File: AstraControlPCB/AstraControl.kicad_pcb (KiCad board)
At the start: 4 copper layers, 102 x 96 mm, 154 parts, among them CN1 4P JST VH, CN10 JST_ZH_6PIN_1A_250V, CN2 4P JST VH, CN3 4P JST VH, CN4 4P JST ZH, CN5 4P JST ZH, CN6 4P JST ZH, CN7 JST_VH_8PIN_10A_250V, CN8 4P JST ZH, CN9 4P JST ZH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

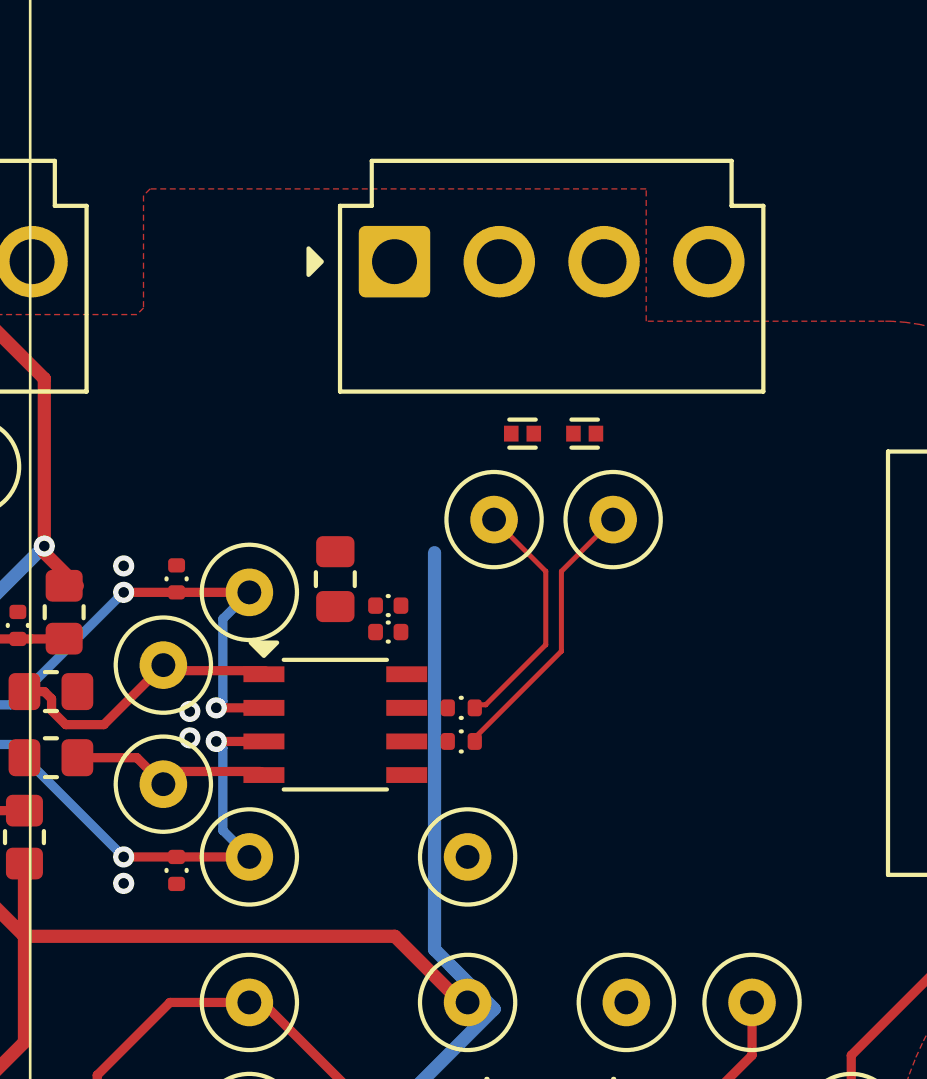
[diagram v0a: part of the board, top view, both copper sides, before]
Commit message: RS485 tranceiver changed and TVS
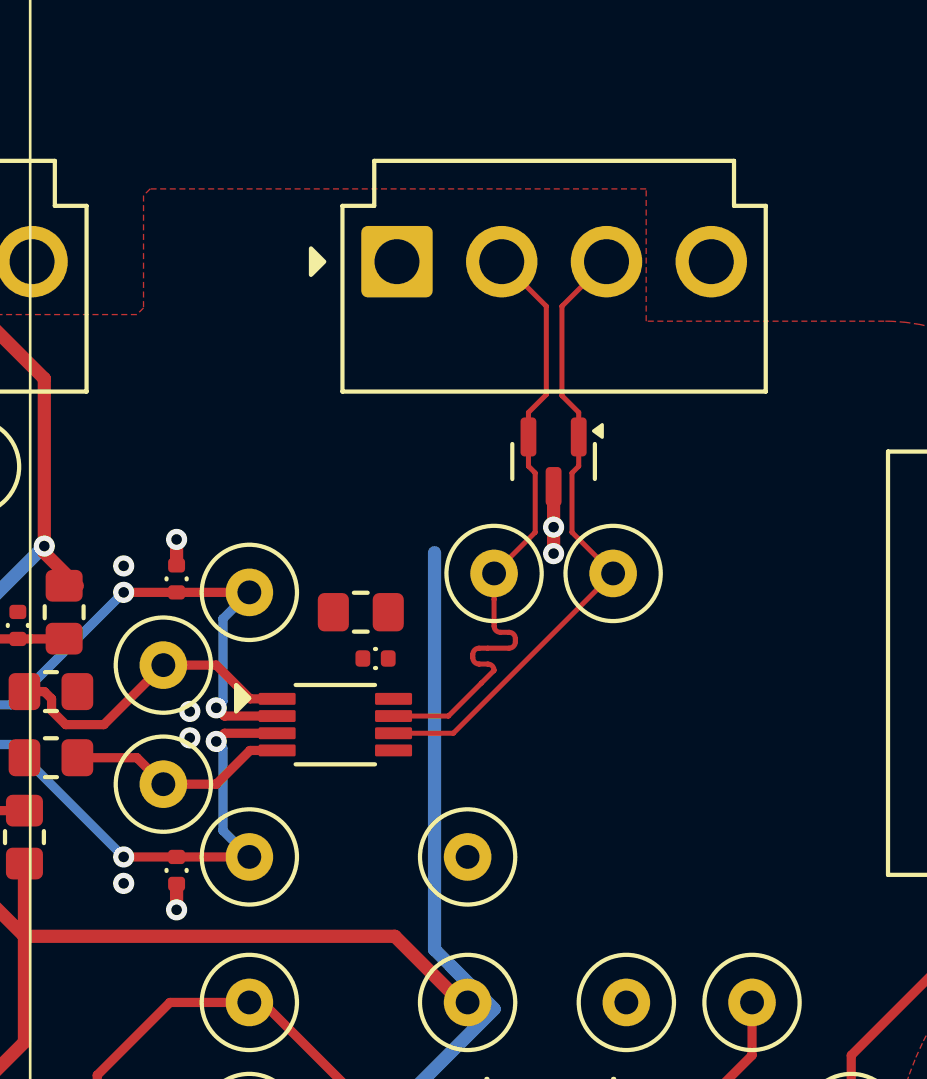
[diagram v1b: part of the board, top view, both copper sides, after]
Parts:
- removed C19: 100n, LiveAstra:C_0402_1005Metric
- removed D2: H5VL10B, LiveAstra:D_DFN0603_H5VL10B_Bidirectional_TVS
- removed R14, R15: 10, LiveAstra:R_0402_1005Metric
- D3: value H5VL10B -> NUP3105LT1G; footprint LiveAstra:D_DFN0603_H5VL10B_Bidirectional_TVS -> LiveAstra:TVS_NUP3105LT1G_36V
- U5: value SN65HVD1782DR -> THVD2450DGKR; footprint LiveAstra:RS_485_SN65HVD1782DR -> LiveAstra:THVD2450DGKR_RS485_Transciever_VSSOP8
- moved TP15 2.03 mm to (172.3, 57.2)
- moved TP16 2.03 mm to (167.8, 57.2)
- moved D3 1.64 mm to (170.0, 53.0), turned to -90 degrees
- moved C17 1.58 mm to (162.7, 58.6), turned to 0 degrees
- moved C18 1.11 mm to (163.3, 60.4)
- moved CN1 0.09 mm to (164.1, 45.4)
- turned U5 to 0 degrees
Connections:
- C17 pad 2: +3V3 -> +5V
- C18 pad 2: +3V3 -> +5V
- CN1 pad 2: /Block Diagram/Power Connectors/RS485_D+ -> /Block Diagram/UART to RS-485/RS485_IC_D+
- CN1 pad 3: /Block Diagram/Power Connectors/RS485_D- -> /Block Diagram/UART to RS-485/RS485_IC_D-
- D3 pad 1: GND -> /Block Diagram/UART to RS-485/RS485_IC_D-
- D3 pad 2: /Block Diagram/Power Connectors/RS485_D- -> /Block Diagram/UART to RS-485/RS485_IC_D+
- TP15 pad 1: /Block Diagram/Power Connectors/RS485_D- -> /Block Diagram/UART to RS-485/RS485_IC_D-
- TP16 pad 1: /Block Diagram/Power Connectors/RS485_D+ -> /Block Diagram/UART to RS-485/RS485_IC_D+
- U5 pad 8: +3V3 -> +5V
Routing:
- net /Block Diagram/UART to RS-485/RS485_IC_D-: track 0.00 -> 24.3 mm
- net /Block Diagram/UART to RS-485/RS485_IC_D+: track 0.00 -> 24.2 mm
- net /Block Diagram/Power Connectors/RS485_D-: track 10.4 -> 0.00 mm
- net /Block Diagram/Power Connectors/RS485_D+: track 9.16 -> 0.00 mm
- net GND: track 20.2 -> 24.7 mm, vias 63 -> 67
- net /Block Diagram/UART to RS-485/RS485_RX_IC: track 11.0 -> 11.9 mm
- net /Block Diagram/UART to RS-485/RS485_TX_IC: track 7.72 -> 8.49 mm
- net /Block Diagram/MCU/GPIO_6_RS485_RE: track 38.1 -> 38.7 mm
- net /Block Diagram/MCU/GPIO_5_RS485_DE: track 35.8 -> 36.4 mm

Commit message: Reroute complete
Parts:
- added C19: 47u, LiveAstra:C_0805_2012Metric_Pad1.18x1.45mm_HandSolder, F.Cu at (144.8, 68.1)
- added C28: DNP, LiveAstra:C_0805_2012Metric_Pad1.18x1.45mm_HandSolder, F.Cu at (173.0, 75.6)
- added R14: 1M, LiveAstra:R_0805_2012Metric_Pad1.20x1.40mm_HandSolder, F.Cu at (179.5, 99.9)
- C1: value 22u -> 47u; footprint LiveAstra:C_0603_1608Metric -> LiveAstra:C_0805_2012Metric_Pad1.18x1.45mm_HandSolder
- moved R45 113.1 mm to (105.8, 111.6), turned to -90 degrees
- moved C25 108.0 mm to (108.8, 111.6), turned to -90 degrees
- moved C24 73.6 mm to (172.8, 37.4), turned to 0 degrees
- moved R44 67.8 mm to (167.5, 37.4), turned to 180 degrees
- moved C27 60.7 mm to (104.6, 48.9), turned to 180 degrees
- moved R47 53.4 mm to (104.5, 51.4), turned to 180 degrees
- moved TP10 53.4 mm to (117.0, 68.1)
- moved TP11 42.4 mm to (104.8, 69.8)
- moved C1 22.9 mm to (163.0, 55.9), turned to 0 degrees
- moved C17 17.5 mm to (166.8, 75.6), turned to 180 degrees
- moved CN4 12.0 mm to (184.3, 119.6)
- moved CN5 12.0 mm to (172.3, 119.6)
- moved TP33 12.0 mm to (167.8, 114.6)
- moved TP35 12.0 mm to (179.8, 114.6)
- moved TP36 12.0 mm to (184.3, 114.6)
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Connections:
- C1 pad 2: +3V3 -> +5V
- C17 pad 2: +5V -> +3V3
- CN1 pad 2: /Block Diagram/UART to RS-485/RS485_IC_D+ -> /Block Diagram/Power Connectors/RS485_D+
- CN1 pad 3: /Block Diagram/UART to RS-485/RS485_IC_D- -> /Block Diagram/Power Connectors/RS485_D-
- D3 pad 1: /Block Diagram/UART to RS-485/RS485_IC_D- -> /Block Diagram/Power Connectors/RS485_D+
- D3 pad 2: /Block Diagram/UART to RS-485/RS485_IC_D+ -> /Block Diagram/Power Connectors/RS485_D-
- TP15 pad 1: /Block Diagram/UART to RS-485/RS485_IC_D- -> /Block Diagram/Power Connectors/RS485_D-
- TP16 pad 1: /Block Diagram/UART to RS-485/RS485_IC_D+ -> /Block Diagram/Power Connectors/RS485_D+
- U1 pad 28: /Block Diagram/Fan, Temperature and Screen/FAN_PWM -> /Block Diagram/Fan, Temperature and Screen/TEMP_I2C_SCL
- U1 pad 29: /Block Diagram/Fan, Temperature and Screen/FAN_TACHO -> /Block Diagram/Fan, Temperature and Screen/TEMP_I2C_SDA
- U1 pad 30: /Block Diagram/Fan, Temperature and Screen/TEMP_I2C_SCL -> /Block Diagram/Fan, Temperature and Screen/FAN_PWM
- U1 pad 31: /Block Diagram/Fan, Temperature and Screen/TEMP_I2C_SDA -> /Block Diagram/Fan, Temperature and Screen/FAN_TACHO
- U2 pad 4: unconnected-(U2-~{FLAG}-Pad4) -> /Block Diagram/5V Protection/FLAG_IC
- U5 pad 6: /Block Diagram/UART to RS-485/RS485_IC_D- -> /Block Diagram/Power Connectors/RS485_D-
- U5 pad 7: /Block Diagram/UART to RS-485/RS485_IC_D+ -> /Block Diagram/Power Connectors/RS485_D+
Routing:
- net +3V3: track 103.4 -> 22.6 mm, vias 12 -> 39
- net GND: track 24.7 -> 65.9 mm, vias 67 -> 125
- net /Block Diagram/UART to RS-485/RS485_IC_D-: track 24.3 -> 0.00 mm
- net /Block Diagram/UART to RS-485/RS485_IC_D+: track 24.2 -> 0.00 mm
- net /Block Diagram/Power Connectors/RS485_D-: track 0.00 -> 24.1 mm
- net /Block Diagram/Power Connectors/RS485_D+: track 0.00 -> 24.0 mm
- net /Block Diagram/3V3 to 5V Logic Shifter/5V_IO_1: track 8.22 -> 26.3 mm
- net /Block Diagram/3V3 to 5V Logic Shifter/5V_IO_4: track 20.5 -> 33.4 mm
- net /Block Diagram/3V3 to 5V Logic Shifter/OE_IC: track 0.00 -> 12.2 mm
- net /Block Diagram/MCU/IO_3_IC: track 0.00 -> 10.0 mm
- net /Block Diagram/5V Protection/FLAG_IC: track 0.00 -> 8.66 mm, vias 0 -> 2
- net CHASSIS: track 0.00 -> 8.37 mm
- net /Block Diagram/3V3 to 5V Logic Shifter/5V_IO_3: track 24.3 -> 32.3 mm
- net /Block Diagram/5V to 3.3V/SW_OUT_UNFILTERED: track 10.2 -> 17.5 mm
- net /Block Diagram/Fan, Temperature and Screen/FAN_TACHO: track 10.8 -> 17.4 mm
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- added copper zone on B.Cu, net +5V
- added copper zone on B.Cu, net +5V_IN
- added copper zone on B.Cu, net /Block Diagram/Power Connectors/USB/VBUS
- added copper zone on F.Cu, net /Block Diagram/Power Connectors/USB/VBUS
- added copper zone on F.Cu, net CHASSIS

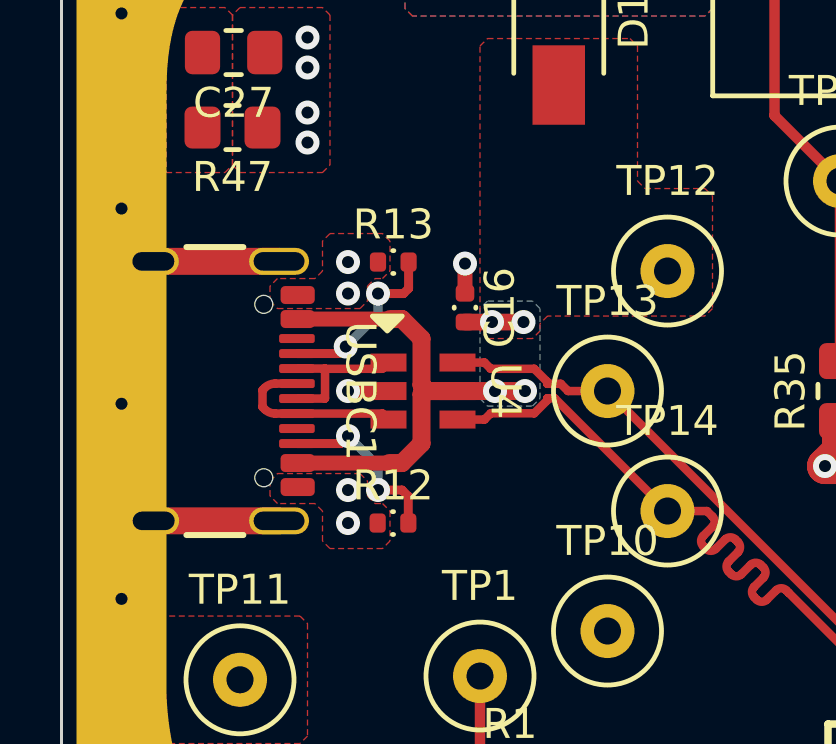
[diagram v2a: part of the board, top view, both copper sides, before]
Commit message: Fixed fab layer
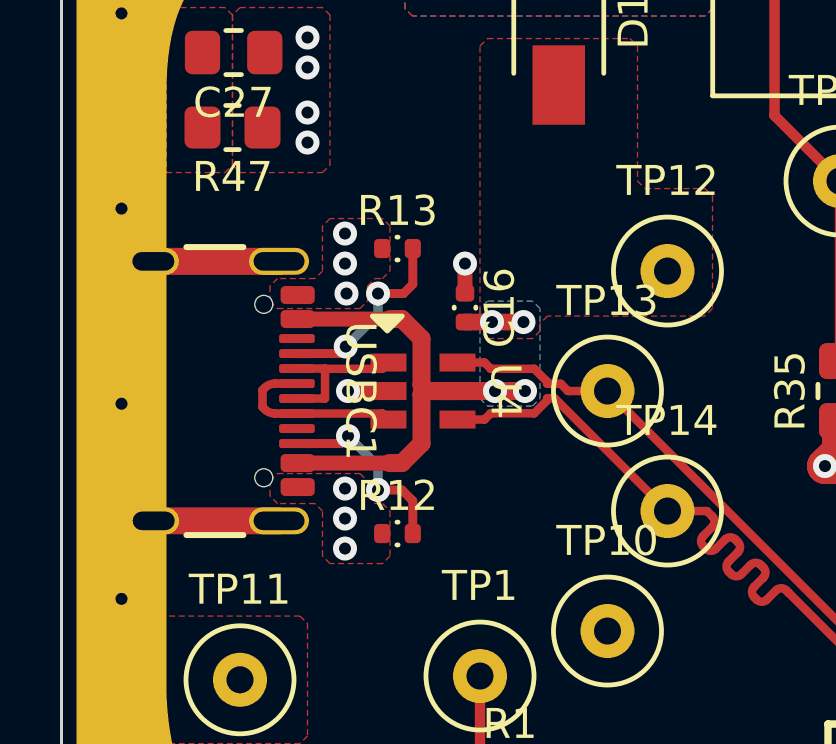
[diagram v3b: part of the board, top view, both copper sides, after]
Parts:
- C12, C15, C17, C28: footprint LiveAstra:C_0805_2012Metric_Pad1.18x1.45mm_HandSolder -> LiveAstra:C_DNP_0805_2012Metric_Pad1.18x1.45mm_HandSolder
- R26, R27, R33, R34, R45, R46, R47, R48, R49: footprint LiveAstra:R_0805_2012Metric_Pad1.20x1.40mm_HandSolder -> LiveAstra:R_DNP_0805_2012Metric_Pad1.20x1.40mm_HandSolder
- moved R13 0.47 mm to (110.0, 55.4)
- moved R12 0.38 mm to (110.0, 64.9)
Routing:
- net /Block Diagram/Power Connectors/USB/CC1: track 5.91 -> 6.41 mm
- net GND: vias 125 -> 127

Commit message: Silkscreen
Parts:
- moved R1 3.72 mm to (117.3, 71.6)
- moved D1 0.16 mm to (115.3, 47.9)
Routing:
- net +3V3: track 22.6 -> 27.0 mm
- net /Block Diagram/MCU/IO_3_IC: track 10.0 -> 7.03 mm
- net /Block Diagram/MCU/IO_3_TEST: track 3.25 -> 4.33 mm
- net /Block Diagram/Fan, Temperature and Screen/TEMP_I2C_SCL: track 67.2 -> 66.2 mm
- net /Block Diagram/Fan, Temperature and Screen/TEMP_I2C_SDA: track 71.7 -> 71.1 mm
- net GND: vias 127 -> 129

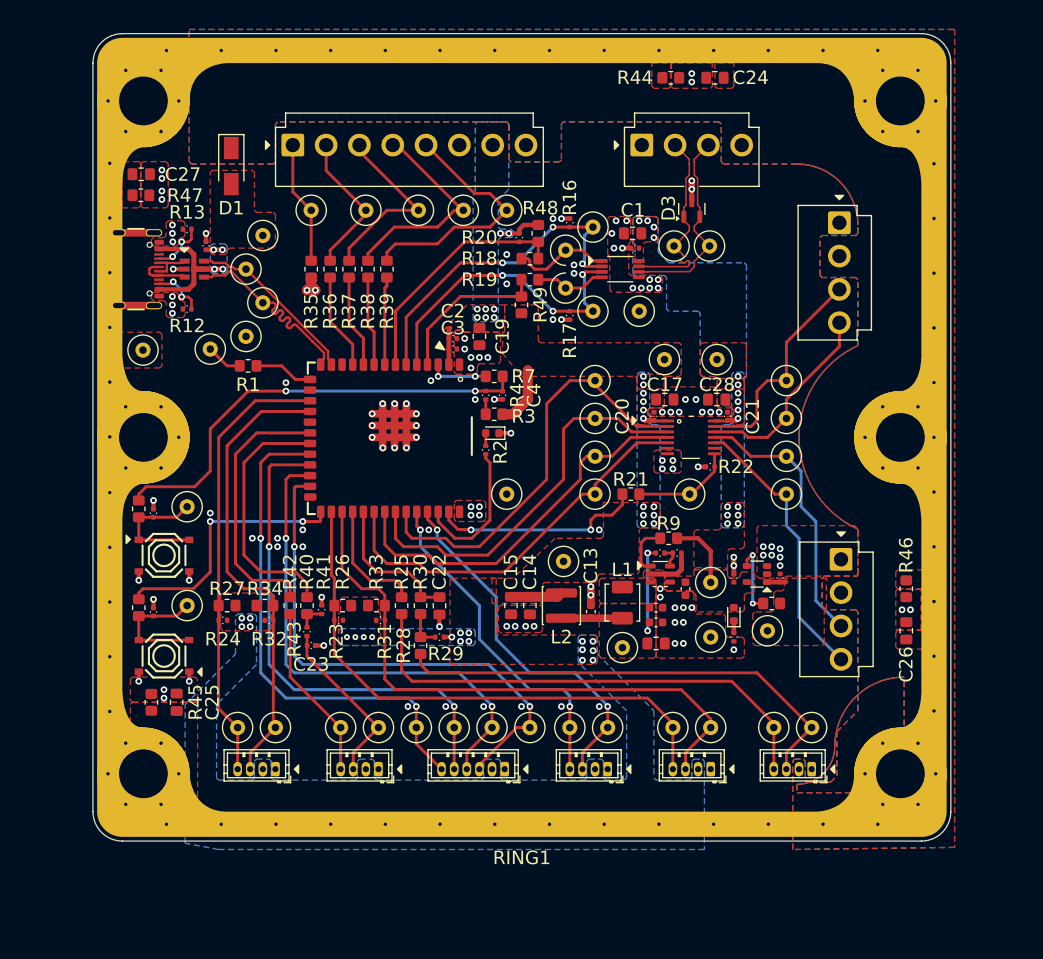
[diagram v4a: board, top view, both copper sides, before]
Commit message: update bottom render, fix center, add gnd pour
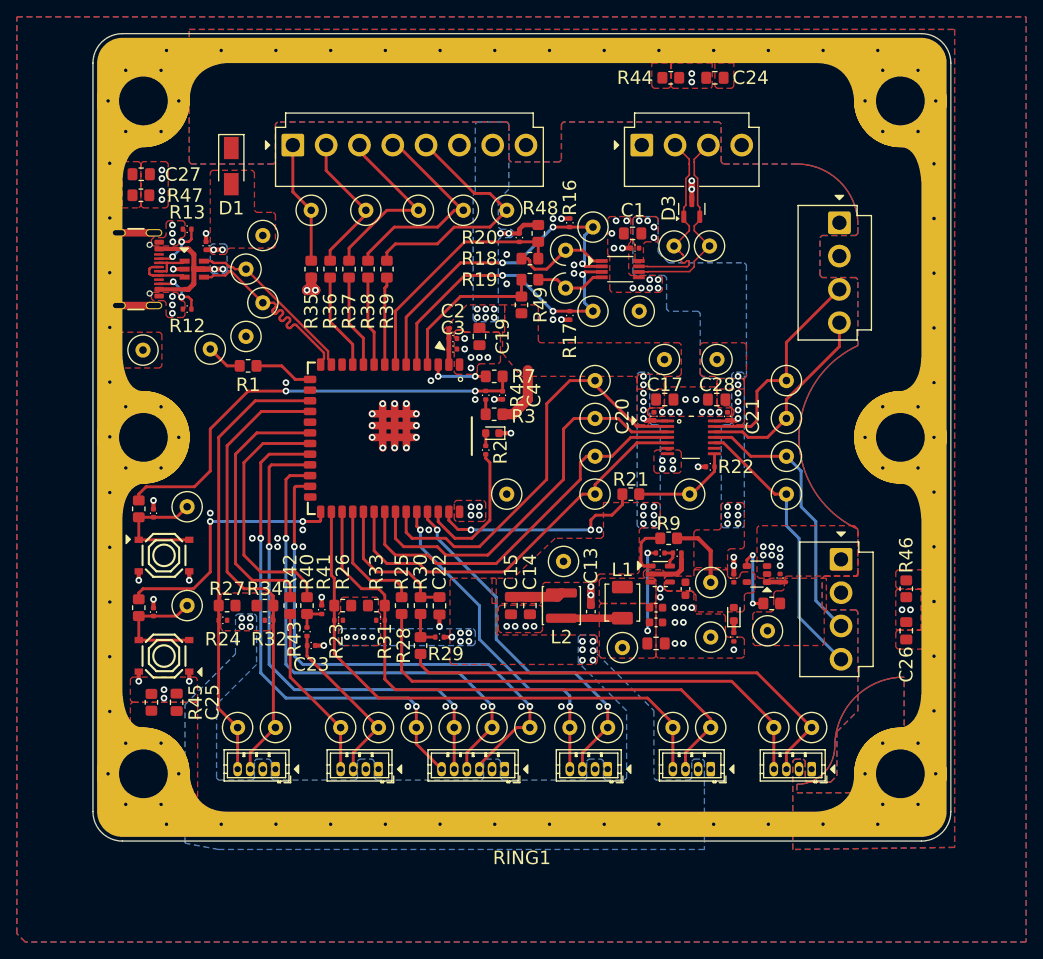
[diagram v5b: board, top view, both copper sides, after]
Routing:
- added copper zone on B.Cu, net GND

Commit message: Fix all DRC
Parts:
- moved TP2 4.92 mm to (150.0, 82.4)
- moved RING1 0.05 mm to (149.8, 80.1)
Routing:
- net GND: vias 129 -> 235
- net +5V_IN: vias 0 -> 34
